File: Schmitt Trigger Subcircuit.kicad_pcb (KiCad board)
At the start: 2 copper layers, 9 parts, among them J1 Screw_Terminal_01x03, J10 Screw_Terminal_01x01, J2 Screw_Terminal_01x03, J3 Screw_Terminal_01x03, J4 Screw_Terminal_01x03, J7 Screw_Terminal_01x01, J8 Screw_Terminal_01x01, J9 Screw_Terminal_01x01, U1 74LV14

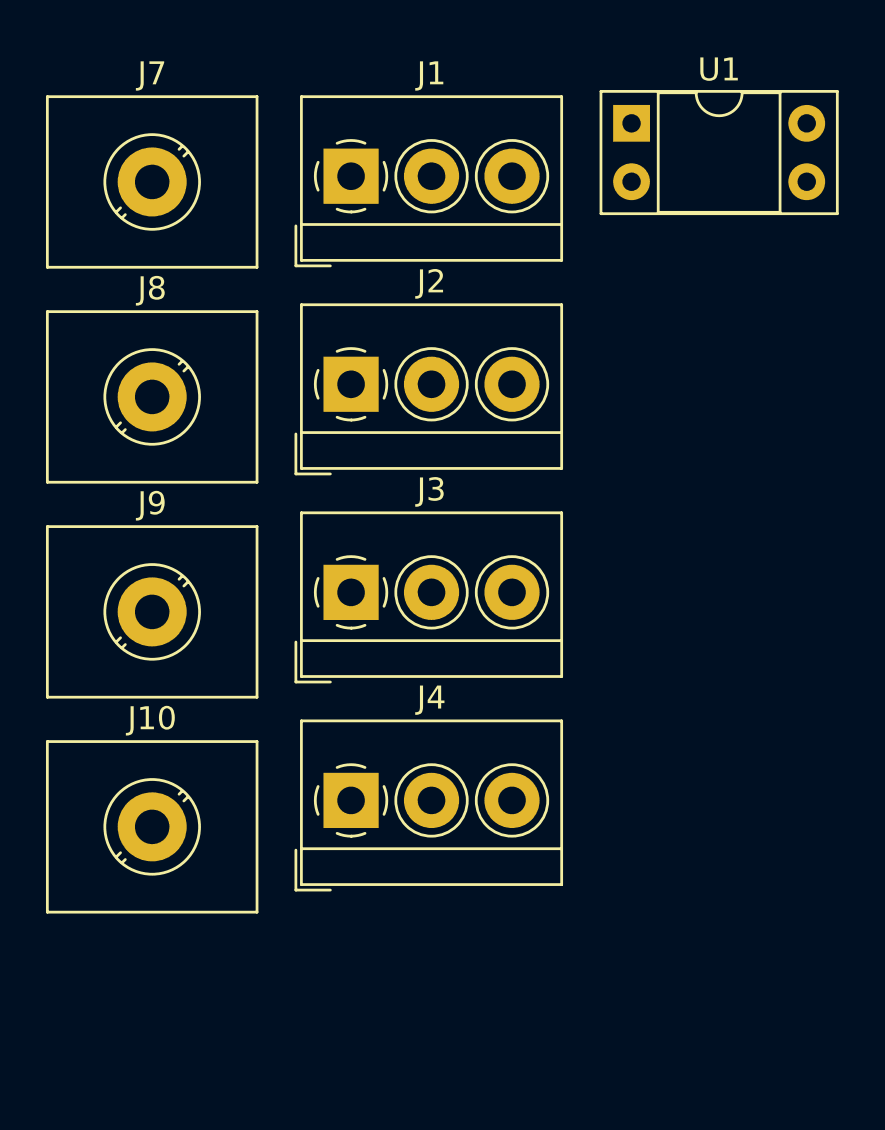
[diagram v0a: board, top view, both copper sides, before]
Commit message: Schmitt Triger Files
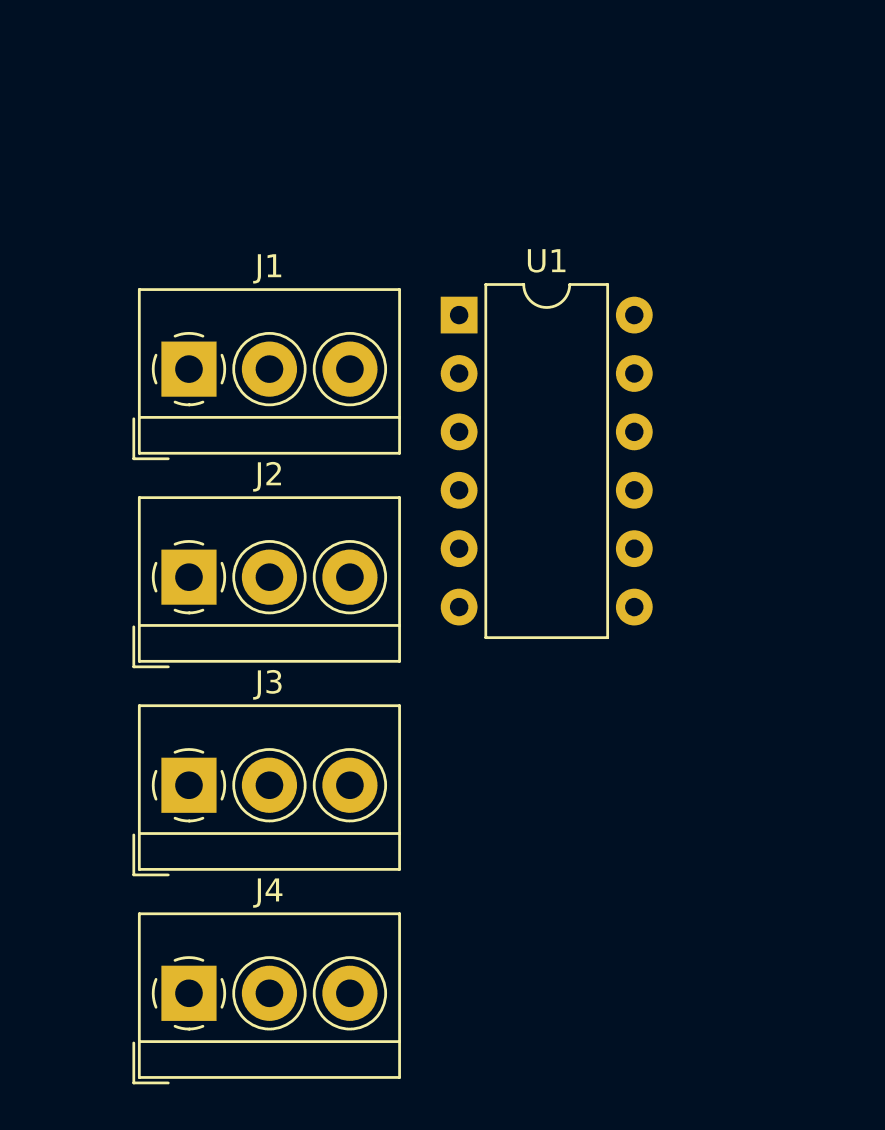
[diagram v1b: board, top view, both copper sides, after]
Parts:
- removed J10, J7, J8, J9: Screw_Terminal_01x01, TerminalBlock_MetzConnect:TerminalBlock_MetzConnect_360271_1x01_Horizontal_ScrewM3.0_Boxed
- U1: footprint Package_DIP:DIP-4_W7.62mm_Socket -> Package_DIP:DIP-12_W7.62mm
- moved U1 11.2 mm to (145.9, 84.3)
- moved J1 11.0 mm to (134.1, 86.7)
- moved J2 11.0 mm to (134.1, 95.7)
- moved J3 11.0 mm to (134.1, 104.8)
- moved J4 11.0 mm to (134.1, 113.8)
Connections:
- U1 pad 2: Net-(J7-Pin_1) -> /Jetson GPIO Pin 1
- U1 pad 4: Net-(J8-Pin_1) -> /Jetson GPIO Pin 2
